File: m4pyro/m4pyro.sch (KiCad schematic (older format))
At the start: 75 parts, among them IC1 MCP2562, J1 WEST TOP, J2 EAST TOP, P1 SWD_TC, Y1 26M

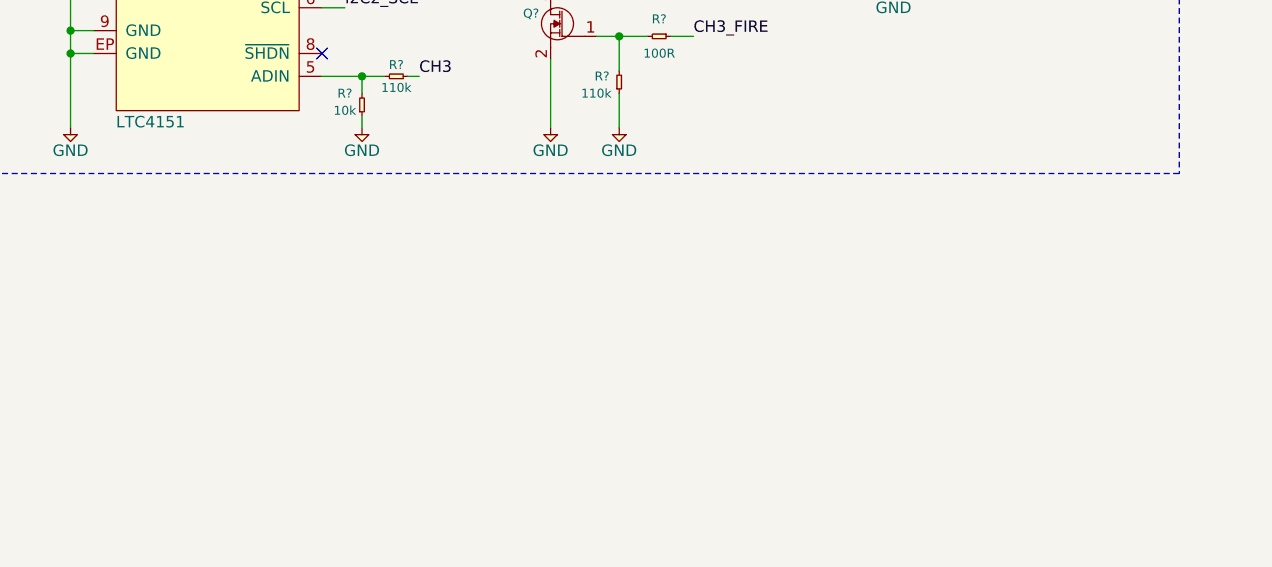
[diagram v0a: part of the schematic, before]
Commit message: Add note of previously suggested modifications
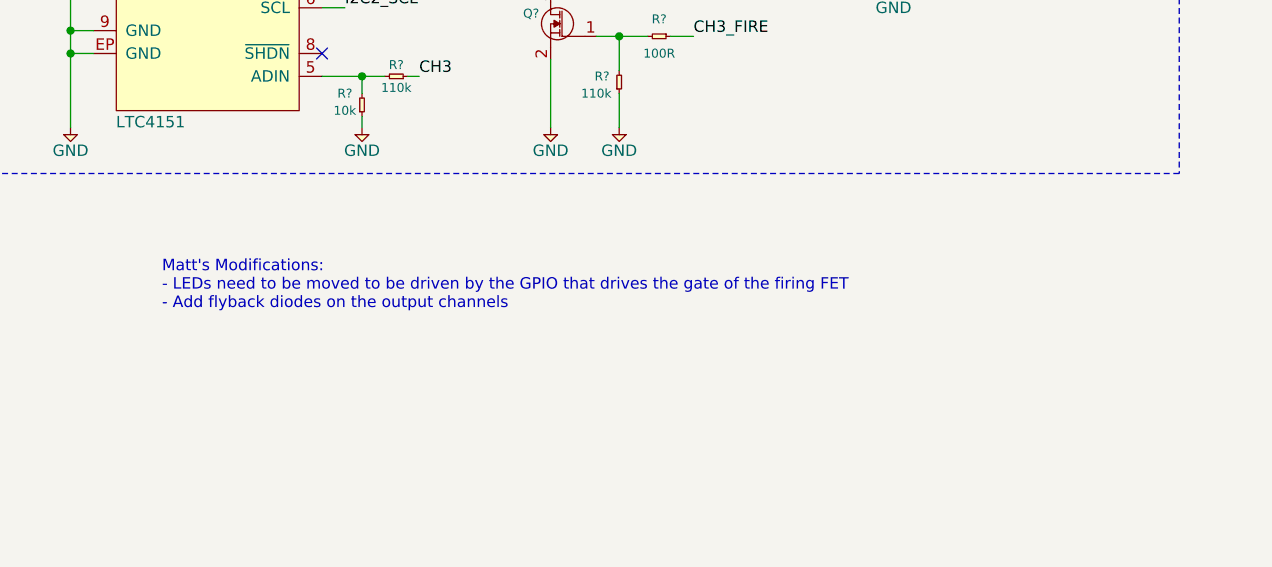
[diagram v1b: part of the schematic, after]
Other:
- note added: "Matt's Modifications:\n- LEDs need to be moved to be driven by the GPIO that drives the gate of the firing FET\n- Add flyback diodes on the output channels"
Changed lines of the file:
@@
 encoding utf-8
 Sheet 1 1
-Title "Martlet IV Pyro"
+Title "M4_PYRO"
 Date "2020-02-05"
 Rev "1"
 Comp "CU Spaceflight"
-Comment1 "Henry Franks"
-Comment2 "Saurav Prakeerth"
-Comment3 "Drawn By:"
+Comment1 "Drawn By: Saurav Prakeerth"
+Comment2 ""
+Comment3 ""
 Comment4 ""
 $EndDescr
@@
 	1    0    0    -1
 $EndComp
+Text Notes 5500 7300 0    50   ~ 0
+Matt's Modifications:\n- LEDs need to be moved to be driven by the GPIO that drives the gate of the firing FET\n- Add flyback diodes on the output channels
 $EndSCHEMATC

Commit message: Align components to grid
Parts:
- removed D? (x3): D, ignition:SOD-123F, symbol cusf-kicad:D
- removed D? (x3): SCHOTTKY, ignition:SOD-123FL, symbol cusf-kicad:SCHOTTKY
- removed IC? (x2): LTC4151, agg:MSOP-10, symbol cusf-kicad:LTC4151
- removed J?: CH2, ignition:172316-1104, symbol cusf-kicad:CONN_01x04
- removed J?: CH1, ignition:172316-1104, symbol cusf-kicad:CONN_01x04
- removed J?: CH3, ignition:172316-1104, symbol cusf-kicad:CONN_01x04
- removed K? (x3): 16A_SPST, symbol cusf-kicad:RELAY_SPST
- removed Q? (x3): NFET, agg:SOT-23, symbol cusf-kicad:NFET
- removed R? (x3): 0.05R, agg:2512, symbol cusf-kicad:R
- removed R? (x6): 10k, agg:0603, symbol cusf-kicad:R
- removed R? (x5): 110k, agg:0603, symbol cusf-kicad:R
- removed R? (x3): 1k, agg:0603, symbol cusf-kicad:R
- removed R? (x2): 100R, agg:0603, symbol cusf-kicad:R
- removed X? (x2): M12 Plug, symbol cusf-kicad:PART
- removed X? (x2): M12 Socket, symbol cusf-kicad:PART
- removed X? (x2): Molex Wire, symbol cusf-kicad:PART
- added D? (x3): SCHOTTKY, ignition:SOD-123FL, symbol cusf-kicad:SCHOTTKY
- added D? (x3): D, ignition:SOD-123F, symbol cusf-kicad:D
- added IC? (x2): LTC4151, agg:MSOP-10, symbol cusf-kicad:LTC4151
- added J? (x3): CH1, ignition:172316-1104, symbol cusf-kicad:CONN_01x04
- added K? (x3): 16A_SPST, symbol cusf-kicad:RELAY_SPST
- added Q? (x3): NFET, agg:SOT-23, symbol cusf-kicad:NFET
- added R? (x6): 10k, symbol cusf-kicad:R
- added R? (x3): 110k, symbol cusf-kicad:R
- added R? (x3): 0.05, symbol cusf-kicad:R
- added R? (x3): 1k, symbol cusf-kicad:R
- added R? (x2): 110k, agg:0603, symbol cusf-kicad:R
- added R? (x2): 100, agg:0603, symbol cusf-kicad:R
- added X? (x2): M12 Plug, symbol cusf-kicad:PART
- added X? (x2): M12 Socket, symbol cusf-kicad:PART
- added X? (x2): Molex Wire, symbol cusf-kicad:PART
- R?: value 100R -> 100
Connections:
- net 3v3: now also D?.1, D?.1, D?.1, R?.1, R?.1, R?.1
- net CH1: now also R?.1
- net CH1_CONT: now also D?.2, R?.1
- net CH2: now also R?.1
- net CH2_CONT: now also D?.2, R?.1
- net CH2_FIRE: now also R?.1
- net CH3: now also R?.1
- net CH3_CONT: now also D?.2, R?.1
- net CH3_FIRE: now also R?.1
- net FIRE_DIST: now also D?.1, D?.1, D?.1, IC?.1 (SENSE+), IC?.1 (SENSE+), IC?.2 (VIN), IC?.2 (VIN), IC?.3 (ADR1), IC?.3 (ADR1), IC?.4 (ADR0), K?.2, K?.2, K?.2, R?.2, R?.2, R?.2
- net GND: now also IC?.4 (ADR0), IC?.9 (GND), IC?.9 (GND), IC?.EP (GND), IC?.EP (GND), J?.3, J?.3, J?.3, J?.4, J?.4, J?.4, Q?.2 (S), Q?.2 (S), Q?.2 (S), R?.1, R?.1, R?.2, R?.2, R?.2
- net I2C2_SCL: now also IC?.6 (SCL), IC?.6 (SCL)
- net I2C2_SDA: now also IC?.7 (SDA), IC?.7 (SDA)
- net at R?.2, R?.2: now also Q?.1 (G)
- net at IC?.10 (SENSE-): now also K?.3, R?.1
- net at IC?.5 (ADIN): now also R?.1, R?.2
- new net: D?.2, K?.1, Q?.3 (D) (x3)
- new net: J?.1, J?.2, K?.4, R?.2, R?.2 (x3)
- new net: IC?.10 (SENSE-), K?.3, R?.1 (x2)
- new net: IC?.5 (ADIN), R?.1, R?.2 (x2)
- new net: Q?.1 (G), R?.2, R?.2 (x2)
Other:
- note added: "ADR: 0xCE"
- note added: "Matt's Modifications:\n- Add flyback diodes on the output channels"
- note removed: "ADC Full Scale Range:\nVin: 102.4 V\nSense: 81.92 mV\nADIN: 2.048 V"
- note removed: "ADR: 0xCE\n"
- note removed: "Matt's Modifications:\n- LEDs need to be moved to be driven by the GPIO that drives the gate of the firing FET\n- Add flyback diodes on the output channels"
- note removed: "Sense Resistor Calcs:\nIs= 1.5 A (nom), 4 A (max) \nVs = 1.5 x 0.05 = 75 mV\nPs = 4 x 4 x 0.05 = 0.8 W"
- note removed: "Voltage Divider Calcs:\nVo = 10/(110+10) x 24 = 2 V"
- moved on the sheet: IC?, R?, X?

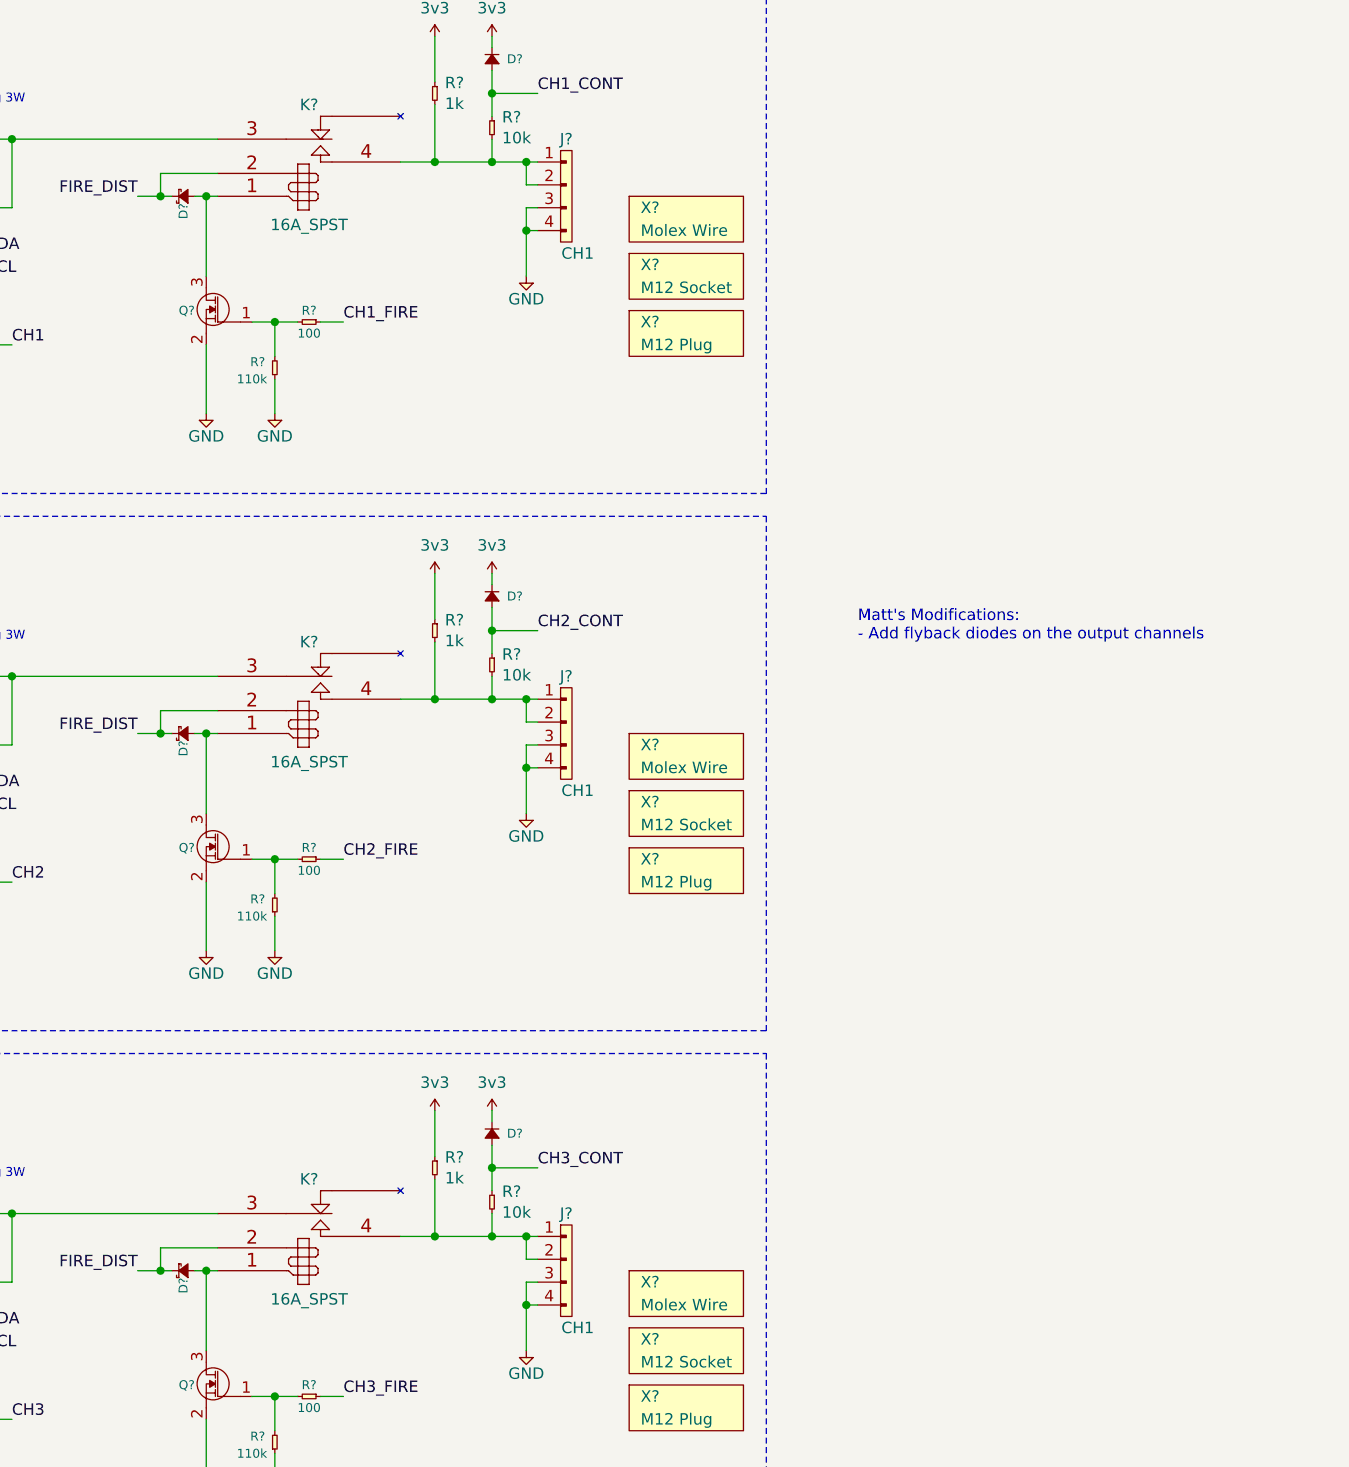
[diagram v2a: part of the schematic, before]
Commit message: Add flyback diodes
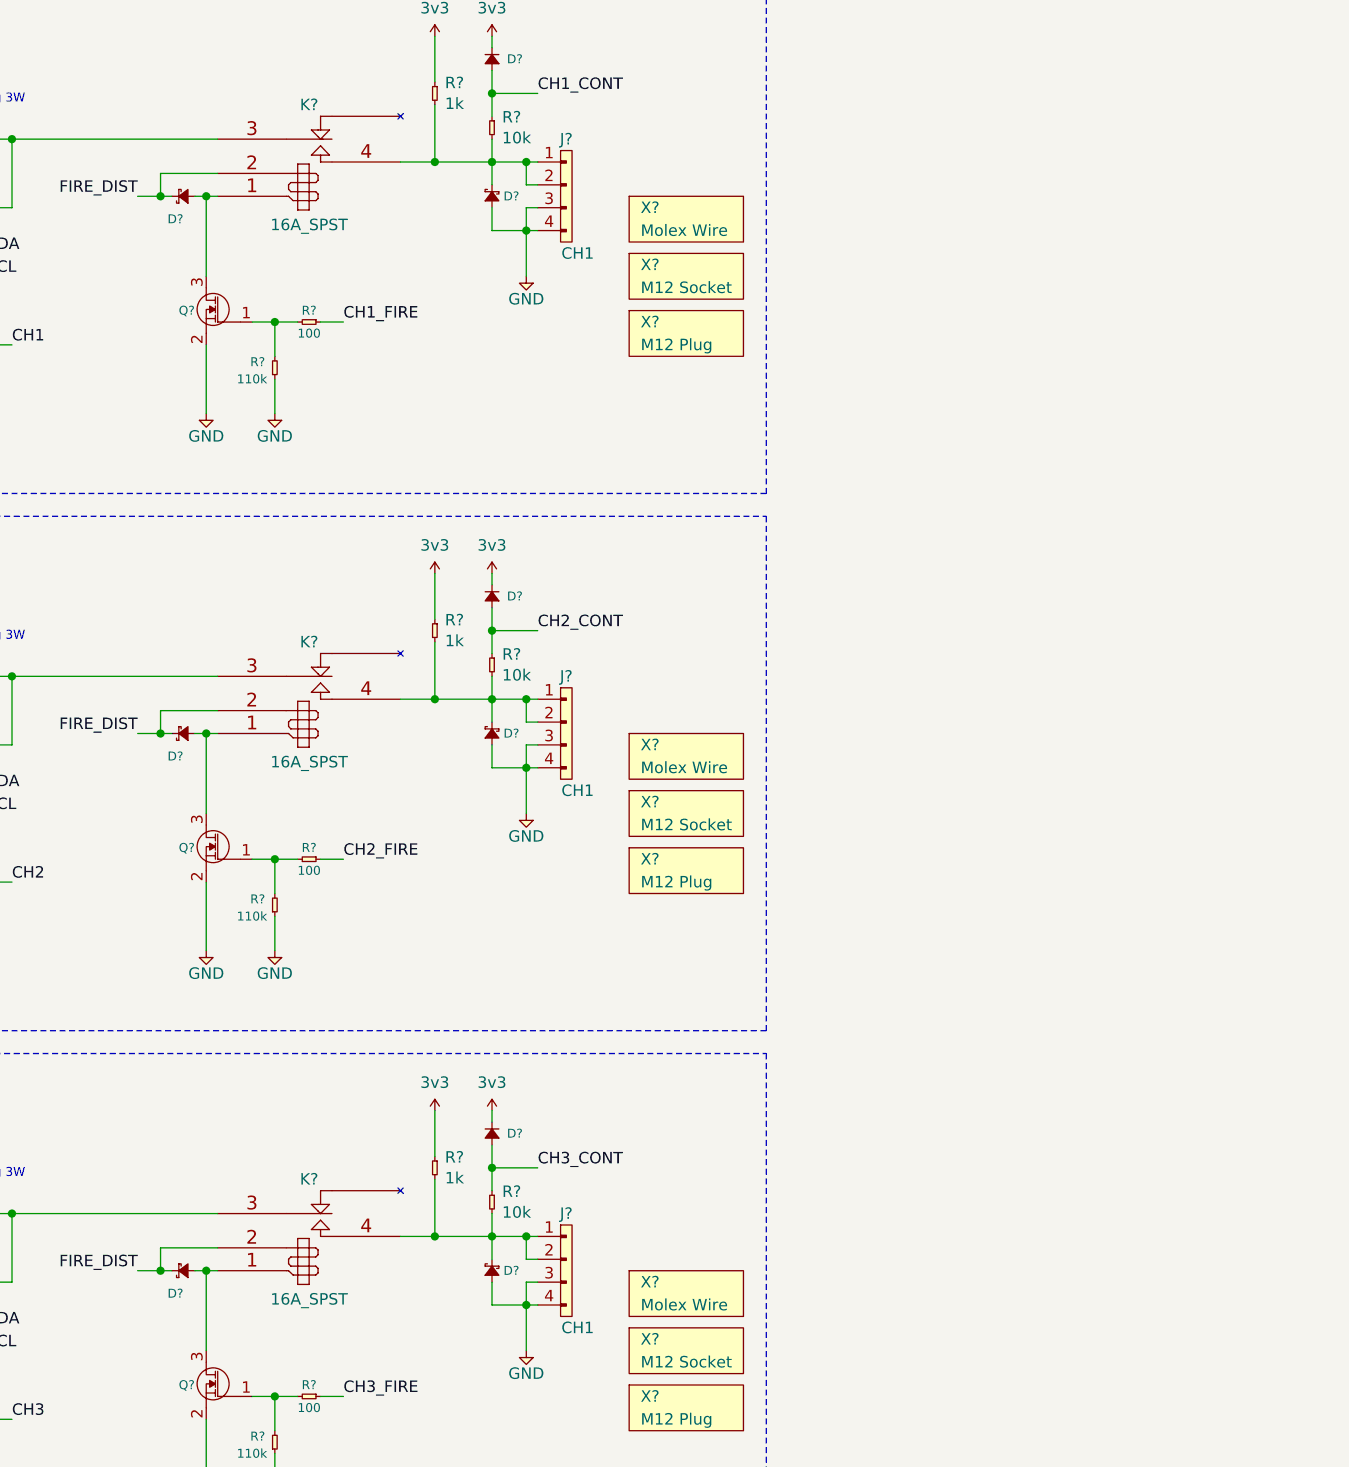
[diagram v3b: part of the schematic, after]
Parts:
- added D? (x3): SCHOTTKY, ignition:SOD-123FL, symbol cusf-kicad:SCHOTTKY
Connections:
- net GND: now also D?.2, D?.2, D?.2
- net at J?.1, J?.2, K?.4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: now also D?.1 (x3)
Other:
- note removed: "Matt's Modifications:\n- Add flyback diodes on the output channels"
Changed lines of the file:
@@
 	1    0    0    -1
 $EndComp
-Text Notes 10250 3700 0    50   ~ 0
-Matt's Modifications:\n- Add flyback diodes on the output channels
 Text Notes 4600 2000 0    50   ~ 0
 ADR: 0xDE
@@
 U 1 1 5EFEB23C
 P 7250 1750
-F 0 "D?" V 7300 1850 39  0000 R CNN
+F 0 "D?" H 7300 1850 39  0000 R CNN
 F 1 "SCHOTTKY" H 7300 1854 50  0001 C CNN
 F 2 "ignition:SOD-123FL" H 7200 1720 50  0001 C CNN
@@
 U 1 1 5F584E1D
 P 7250 4100
-F 0 "D?" V 7300 4200 39  0000 R CNN
+F 0 "D?" H 7300 4200 39  0000 R CNN
 F 1 "SCHOTTKY" H 7300 4204 50  0001 C CNN
 F 2 "ignition:SOD-123FL" H 7200 4070 50  0001 C CNN
@@
 U 1 1 5F5E593E
 P 7250 6450
-F 0 "D?" V 7300 6550 39  0000 R CNN
+F 0 "D?" H 7300 6550 39  0000 R CNN
 F 1 "SCHOTTKY" H 7300 6554 50  0001 C CNN
 F 2 "ignition:SOD-123FL" H 7200 6420 50  0001 C CNN
@@
 Wire Wire Line
 	7400 1750 7400 2100
+Wire Wire Line
+	8650 6400 8650 6300
+Wire Wire Line
+	8650 6500 8650 6600
+Wire Wire Line
+	8650 6600 8800 6600
+Wire Wire Line
+	8650 4050 8650 3950
+Wire Wire Line
+	8650 4150 8650 4250
+Wire Wire Line
+	8650 4250 8800 4250
+Wire Wire Line
+	8650 1700 8650 1600
+Wire Wire Line
+	8650 1800 8650 1900
+Wire Wire Line
+	8650 1900 8800 1900
+$Comp
+L cusf-kicad:SCHOTTKY D?
+U 1 1 5F757D9F
+P 8650 1700
+F 0 "D?" V 8700 1650 39  0000 R CNN
+F 1 "SCHOTTKY" H 8700 1804 50  0001 C CNN
+F 2 "ignition:SOD-123FL" H 8600 1670 50  0001 C CNN
+F 3 "" H 8700 1770 50  0001 C CNN
+F 4 "2452032" H 8650 1700 50  0001 C CNN "Farnell"
+	1    8650 1700
+	0    -1   1    0
+$EndComp
+$Comp
+L cusf-kicad:SCHOTTKY D?
+U 1 1 5F75859A
+P 8650 4050
+F 0 "D?" V 8700 4000 39  0000 R CNN
+F 1 "SCHOTTKY" H 8700 4154 50  0001 C CNN
+F 2 "ignition:SOD-123FL" H 8600 4020 50  0001 C CNN
+F 3 "" H 8700 4120 50  0001 C CNN
+F 4 "2452032" H 8650 4050 50  0001 C CNN "Farnell"
+	1    8650 4050
+	0    -1   1    0
+$EndComp
+$Comp
+L cusf-kicad:SCHOTTKY D?
+U 1 1 5F759023
+P 8650 6400
+F 0 "D?" V 8700 6350 39  0000 R CNN
+F 1 "SCHOTTKY" H 8700 6504 50  0001 C CNN
+F 2 "ignition:SOD-123FL" H 8600 6370 50  0001 C CNN
+F 3 "" H 8700 6470 50  0001 C CNN
+F 4 "2452032" H 8650 6400 50  0001 C CNN "Farnell"
+	1    8650 6400
+	0    -1   1    0
+$EndComp
 $EndSCHEMATC
